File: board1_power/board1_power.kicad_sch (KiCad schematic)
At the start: 0 parts

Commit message: board1_power: migrate drawn capture (USB_IN + 4x charge channel)
- Bring USB_IN and charge_chanel sheets forward from the archived single-board
  design into the live board1_power project; archive copy stays frozen.
- Fix library references: lib_id and footprint nicknames AURC_BMS:/easyeda2kicad:
  -> BMS:; project-name strings -> board1_power; register sheet hierarchy in
  board1_power.kicad_pro.
- Validated with kicad-cli sch erc: hierarchy loads, all BMS: symbols + footprints
  resolve. Remaining 169 violations are work-in-progress (unconnected pins, missing
  PWR_FLAGs, Unspecified pin-type warnings from imported symbols) — pre-existing
  capture state, not migration defects.
- Capture plan annotated with build status + remaining GUI steps.

Co-Authored-By: Claude Opus 4.8 (1M context) <noreply@anthropic.com>
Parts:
- added C1, C2: 1uF, Capacitor_SMD:C_0805_2012Metric, symbol Device:C
- added C27: C, symbol Device:C
- added C28: 0.1uF, symbol Device:C
- added JP1: Jumper_2_Small_Open, TestPoint:TestPoint_2Pads_Pitch2.54mm_Drill0.8mm, symbol Jumper:Jumper_2_Small_Open
- added R1: 100K, symbol Device:R
- added R2: 0R, symbol Device:R
- added R3: 33K, symbol Device:R
- added R4: R, symbol Device:R
- added R41, R44: 10K, symbol Device:R
- added R42, R43: 4.7K, symbol Device:R
- added U1: AP2112K-3.3, Package_TO_SOT_SMD:SOT-23-5, symbol Regulator_Linear:AP2112K-3.3
- added U2: ESP32-C3-WROOM-02, RF_Module:ESP32-C3-WROOM-02, symbol RF_Module:ESP32-C3-WROOM-02
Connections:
- new net: R1.2, R2.2, R3.1, U1.3 (EN)
- new net: C28.2, R41.1, U2.2 (EN)
- new net +3V3: C2.1, R41.2, R42.1, R43.2, R44.2, U1.5 (VOUT), U2.1 (3V3)
- new net GND: C1.2, C2.2, C28.1, R3.2, U1.2 (GND), U2.19 (GND), U2.9 (GND)
- new net MUX_RST: R44.1, U2.10 (IO10)
- new net SCL: R43.1, U2.6 (IO7)
- new net SDA: R42.2, U2.5 (IO6)
- new net SYS: C1.1, R2.1, U1.1 (VIN)
- new net SoC LED 1: U2.18 (IO0)
- new net SoC LED 2: U2.17 (IO1)
- new net SoC LED 3: U2.15 (IO3)
- new net SoC LED 4: U2.3 (IO4)
- new net USB_N: U2.13 (IO18)
- new net USB_P: U2.14 (IO19)
- new net VBUS: R1.1
- new net heartbeat LED: U2.4 (IO5)
- no-connect marks 0 -> 1
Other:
- added sheet Charge_Chanel1 (FC1) (charge_chanel.kicad_sch)
- added sheet Charge_Chanel2 (FC2) (charge_chanel.kicad_sch)
- added sheet Charge_Chanel3(PYRO1) (charge_chanel.kicad_sch)
- added sheet Charge_Chanel4(PYRO2) (charge_chanel.kicad_sch)
- added sheet USB_IN (USB_IN.kicad_sch)
- note added: "3V3 Power"
- note added: "Add 0R to enable always on ESP for data streaming"

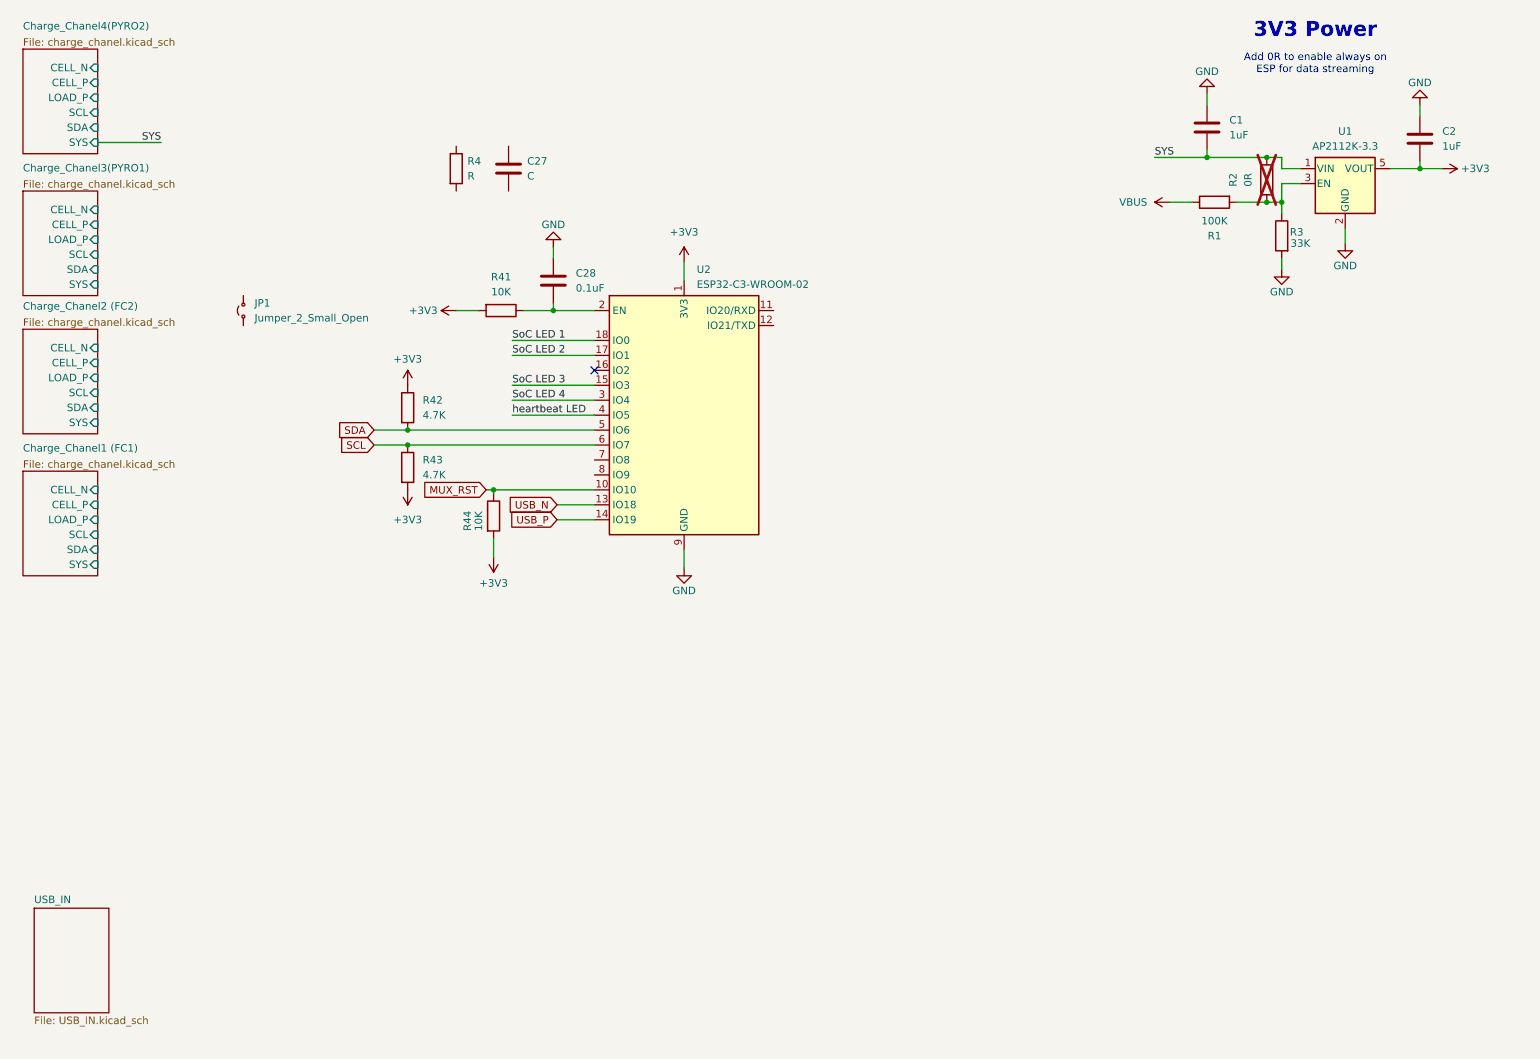
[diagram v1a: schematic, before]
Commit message: board1_power: SYS-default channel rework + ESP32-S3 + mux + connectors
Channel (charge_chanel.kicad_sch):
- Reverse-polarity P-FET (DMG2305UX) moved to cell terminal, drain-to-battery;
  charger BAT on CELL_P_PROT, DW01A sense stays on raw CELL_P.
- 0R source selector (R_SYS populated / R_LOAD DNP, both 2010) -> CHn_V_pre,
  PTC relocated after it -> CH_V output. Old Q2/Q3 reverse FETs removed.
- Bootstrap cap 47nF, PMID 6.8uF. Per-cell SK6812 RGB on LED_VDD=CH1_V chain.

Root (board1_power.kicad_sch):
- ESP32-C3 -> ESP32-S3-WROOM-1. SDA=IO8, SCL=IO9, MUX_RST=IO10(+TCA9548A RESET),
  RGB_DATA=IO48 via 330R, USB=IO19/20, boot IO0=pull-up+JP1, heartbeat=IO2.
- Fixed IO45 strapping pin (was tied to +3V3 -> would force 1.8V flash; now NC).
- TCA9548A mux with per-channel I2C (CH1..4_SDA/SCL). 4.7k pull-ups on main bus.
- J2 power 8-pin (CH1..4_V + GND) and J3 signal 4-pin (SDA/SCL/CH_LIVE/SGND),
  both per interconnect.md.

Library: added DMG2305UX (P-FET, SOT-23) to libs/BMS.kicad_sym.

WIP remaining: PWR_FLAGs, no-connect on last RGB DOUT, drop stray CH3_GND label,
cell holders (CELL_P/N left floating by design), optional TPS22917 ESP gate.

Co-Authored-By: Claude Opus 4.8 (1M context) <noreply@anthropic.com>
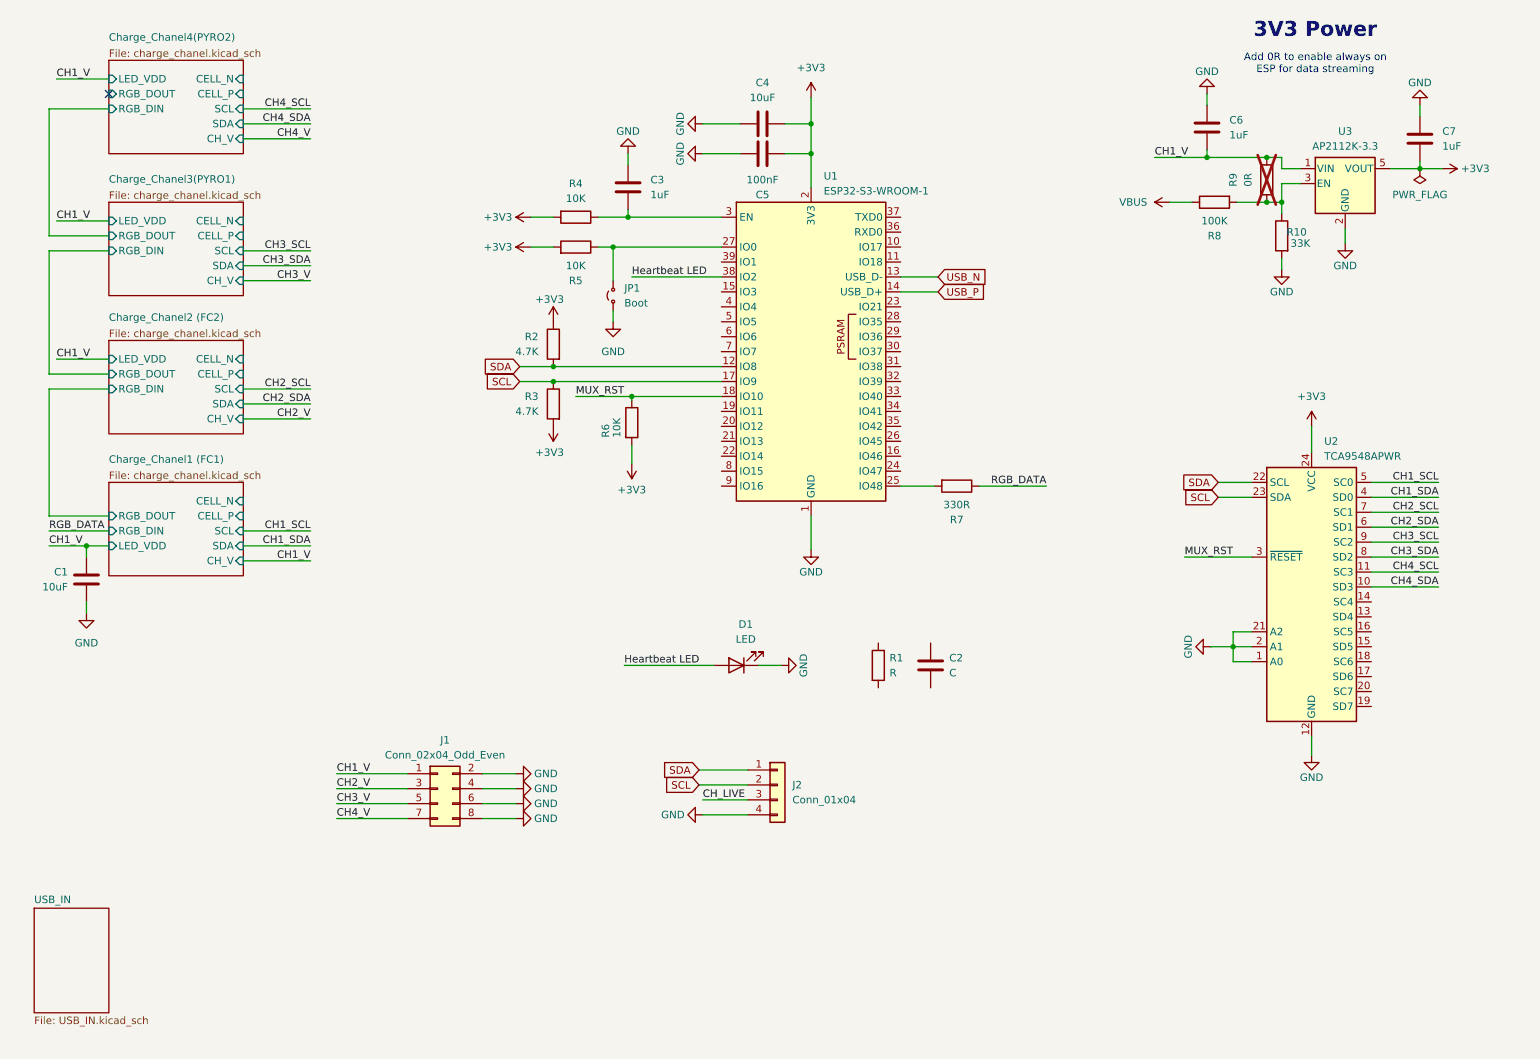
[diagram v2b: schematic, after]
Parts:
- removed U2: ESP32-C3-WROOM-02, RF_Module:ESP32-C3-WROOM-02, symbol RF_Module:ESP32-C3-WROOM-02
- added C1, C4: 10uF, Capacitor_SMD:C_0805_2012Metric, symbol Device:C
- added C5: 100nF, Capacitor_SMD:C_0603_1608Metric, symbol Device:C
- added D1: LED, symbol Device:LED
- added J1: Conn_02x04_Odd_Even, Connector_PinHeader_2.54mm:PinHeader_2x04_P2.54mm_Horizontal, symbol Connector_Generic:Conn_02x04_Odd_Even
- added J2: Conn_01x04, symbol Connector_Generic:Conn_01x04
- added R5: 10K, Resistor_SMD:R_0603_1608Metric, symbol Device:R
- added R7: 330R, Resistor_SMD:R_0603_1608Metric, symbol Device:R
- added U1: ESP32-S3-WROOM-1, RF_Module:ESP32-S3-WROOM-1, symbol RF_Module:ESP32-S3-WROOM-1
- added U2: TCA9548APWR, Package_SO:TSSOP-24_4.4x7.8mm_P0.65mm, symbol Interface_Expansion:TCA9548APWR
- C3: renamed from C28; value 0.1uF -> 1uF; footprint (none) -> Capacitor_SMD:C_0603_1608Metric
- JP1: value Jumper_2_Small_Open -> Boot
- R4: renamed from R41; footprint (none) -> Resistor_SMD:R_0603_1608Metric
- renumbered C27 to C2, C1 to C6, C2 to C7, R4 to R1, R3 to R10, R42 to R2, R43 to R3, R44 to R6, R1 to R8, R2 to R9, U1 to U3
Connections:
- net +3V3: now also C4.1, C5.1, R5.2, U1.2 (3V3), U2.24 (VCC)
- net GND: now also JP1.1 (A), C1.2, C4.2, C5.2, D1.1 (K), J1.2 (Pin_2), J1.4 (Pin_4), J1.6 (Pin_6), J1.8 (Pin_8), J2.4 (Pin_4), U1.1 (GND), U1.40 (GND), U1.41 (GND), U2.1 (A0), U2.12 (GND), U2.2 (A1), U2.21 (A2)
- net MUX_RST: now also U1.18 (IO10), U2.3 (~{RESET})
- net SCL: now also J2.2 (Pin_2), U1.17 (IO9), U2.23 (SDA)
- net SDA: now also J2.1 (Pin_1), U1.12 (IO8), U2.22 (SCL)
- net USB_N: now also U1.13 (USB_D-)
- net USB_P: now also U1.14 (USB_D+)
- net at C3.2, R4.1: now also U1.3 (EN)
- net at JP1.2 (B): now also R5.1, U1.27 (IO0)
- net SYS renamed CH1_V
- net CH1_V: now also C1.1, J1.1 (Pin_1)
- new net: R7.2, U1.25 (IO48)
- new net CH1_SCL: U2.5 (SC0)
- new net CH1_SDA: U2.4 (SD0)
- new net CH2_SCL: U2.7 (SC1)
- new net CH2_SDA: U2.6 (SD1)
- new net CH2_V: J1.3 (Pin_3)
- new net CH3_SCL: U2.9 (SC2)
- new net CH3_SDA: U2.8 (SD2)
- new net CH3_V: J1.5 (Pin_5)
- new net CH4_SCL: U2.11 (SC3)
- new net CH4_SDA: U2.10 (SD3)
- new net CH4_V: J1.7 (Pin_7)
- new net CH_LIVE: J2.3 (Pin_3)
- new net Heartbeat LED: D1.2 (A), U1.38 (IO2)
- new net RGB_DATA: R7.1
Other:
- sheet Charge_Chanel1 (FC1) ports: added CH_V, LED_VDD, RGB_DIN, RGB_DOUT; removed LOAD_P, SYS
- sheet Charge_Chanel2 (FC2) ports: added CH_V, LED_VDD, RGB_DIN, RGB_DOUT; removed LOAD_P, SYS
- sheet Charge_Chanel3(PYRO1) ports: added CH_V, LED_VDD, RGB_DIN, RGB_DOUT; removed LOAD_P, SYS
- sheet Charge_Chanel4(PYRO2) ports: added CH_V, LED_VDD, RGB_DIN, RGB_DOUT; removed LOAD_P, SYS
- moved on the sheet: C2, C3, JP1, R1, R2, R3, R4, R6

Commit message: board1_power: enable network corrected + all footprints assigned (schematic complete)
- ESP enable rebuilt as a proper diode-OR + shunt:
  * MMBD4448HCQW (D12) quad common-cathode diode-OR -> EN, sources =
    {VBUS divider, CH1_V always-on strap (R59 now 100k), WAKE via 10k, self-hold}
  * R60 100k pull-down on EN (default off)
  * Q9 (2N7002) shunt: Drain->EN, Source->GND, Gate->off-header J4 (CH1_V when in)
  * off-header in -> ESP off (storage); out -> ESP on (launch)
- Assigned footprints to the remaining 26 parts (R/C -> 0603, D1 LED, J2 signal
  connector placeholder); channel-sheet parts apply across all 4 instances.

Remaining ERC items are benign/intentional (Unspecified-pin warnings from imported
symbols, floating cell pins until holder, missing PWR_FLAGs/no-connects).

Co-Authored-By: Claude Opus 4.8 (1M context) <noreply@anthropic.com>
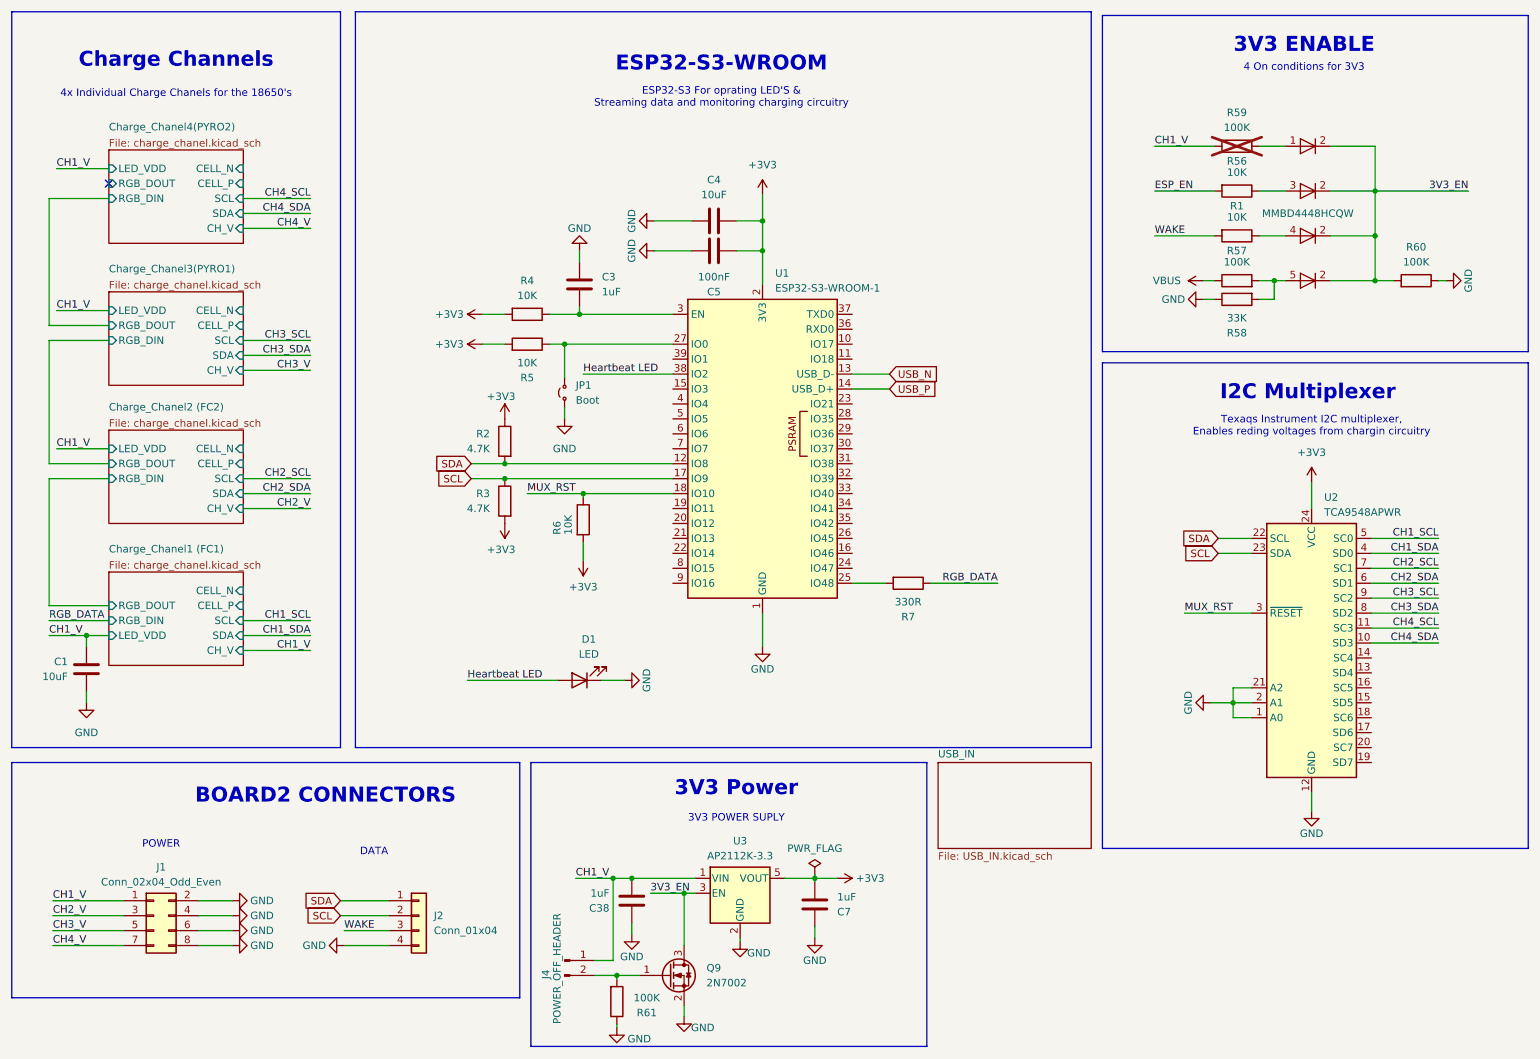
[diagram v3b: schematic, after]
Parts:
- removed C2: C, symbol Device:C
- removed C6: 1uF, Capacitor_SMD:C_0805_2012Metric, symbol Device:C
- removed R10: 33K, symbol Device:R
- removed R8: 100K, symbol Device:R
- removed R9: 0R, symbol Device:R
- added C38: 1uF, Capacitor_SMD:C_0805_2012Metric, symbol Device:C
- added D12: MMBD4448HCQW, Package_TO_SOT_SMD:SOT-353_SC-70-5, symbol Diode:MMBD4448HCQW
- added J4: POWER_OFF_HEADER, Connector_PinHeader_2.54mm:PinHeader_1x02_P2.54mm_Horizontal, symbol Connector:Conn_01x02_Pin
- added Q9: 2N7002, Package_TO_SOT_SMD:SOT-23, symbol Transistor_FET:2N7002
- added R56: 10K, Resistor_SMD:R_0603_1608Metric, symbol Device:R
- added R57, R59, R60, R61: 100K, Resistor_SMD:R_0603_1608Metric, symbol Device:R
- added R58: 33K, Resistor_SMD:R_0603_1608Metric, symbol Device:R
- D1: footprint (none) -> LED_SMD:LED_0603_1608Metric
- J2: footprint (none) -> Connector_PinHeader_2.54mm:PinHeader_1x04_P2.54mm_Horizontal
- R1: value R -> 10K; footprint (none) -> Resistor_SMD:R_0603_1608Metric
- R2, R3, R6: footprint (none) -> Resistor_SMD:R_0603_1608Metric
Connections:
- net CH_LIVE is gone; now on net WAKE: J2.3 (Pin_3)
- net CH1_V: now also C38.1, J4.1 (Pin_1), R59.1
- net GND: now also C38.2, Q9.2 (S), R58.1, R60.1, R61.1
- net VBUS: now also R57.1
- net 3V3_EN: now reaches U3.3 (EN)
- net 3V3_EN: now also D12.2 (K), D12.2 (K), D12.2 (K), D12.2 (K), Q9.3 (D), R60.2
- net at R1.1: now also D12.4 (A)
- net WAKE: now reaches R1.2
- new net: D12.5 (A), R57.2, R58.2
- new net: J4.2 (Pin_2), Q9.1 (G), R61.2
- new net: D12.3 (A), R56.1
- new net: D12.1 (A), R59.2
- new net ESP_EN: R56.2
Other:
- note added: "3V3 ENABLE"
- note added: "3V3 POWER SUPLY"
- note added: "4 On conditions for 3V3"
- note added: "4x Individual Charge Chanels for the 18650's"
- note added: "BOARD2 CONNECTORS"
- note added: "Charge Channels"
- note added: "DATA"
- note added: "ESP32-S3 For oprating LED'S & Streaming data and monitoring charging circuitry"
- note added: "ESP32-S3-WROOM"
- note added: "I2C Multiplexer"
- note added: "POWER"
- note added: "Texaqs Instrument I2C multiplexer, Enables reding voltages from chargin circuitry"
- note removed: "Add 0R to enable always on ESP for data streaming"
- moved on the sheet: C1, C3, C4, C5, C7, D1, J1, J2, JP1, R2, R3, R4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

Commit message: board1_power: PCB footprint placement + layout updates
Co-Authored-By: Claude Opus 4.8 (1M context) <noreply@anthropic.com>
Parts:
- added J5: BH-18650-A1BJ024, BMS:BH-18650-A1BJ024, symbol BMS:BH-18650-A1BJ024
- C5: footprint Capacitor_SMD:C_0603_1608Metric -> Capacitor_SMD:C_0805_2012Metric
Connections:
- net CH1_SCL: now also U2.11 (SC3); no longer U2.5 (SC0)
- net CH1_SDA: now also U2.10 (SD3); no longer U2.4 (SD0)
- net CH1_V: now also J1.7 (Pin_7); no longer J1.1 (Pin_1)
- net CH2_SCL: now also U2.9 (SC2); no longer U2.7 (SC1)
- net CH2_SDA: now also U2.8 (SD2); no longer U2.6 (SD1)
- net CH2_V: now also J1.5 (Pin_5); no longer J1.3 (Pin_3)
- net CH3_SCL: now also U2.7 (SC1); no longer U2.9 (SC2)
- net CH3_SDA: now also U2.6 (SD1); no longer U2.8 (SD2)
- net CH3_V: now also J1.3 (Pin_3); no longer J1.5 (Pin_5)
- net CH4_SCL: now also U2.5 (SC0); no longer U2.11 (SC3)
- net CH4_SDA: now also U2.4 (SD0); no longer U2.10 (SD3)
- net CH4_V: now also J1.1 (Pin_1); no longer J1.7 (Pin_7)
- net ESP_EN: now also U1.10 (IO17)
- new net CH1_CN: J5.5 (N1)
- new net CH1_CP: J5.1 (P1)
- new net CH2_CN: J5.6 (N2)
- new net CH2_CP: J5.2 (P2)
- new net CH3_CN: J5.7 (N3)
- new net CH3_CP: J5.3 (P3)
- new net CH4_CN: J5.8 (N4)
- new net CH4_CP: J5.4 (P4)
- no-connect marks 1 -> 28
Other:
- note added: "18650 HOLDER"
- moved on the sheet: C1, J1, J2
